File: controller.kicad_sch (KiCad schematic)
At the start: 17 parts, among them J701 Debug, SW701 RST, U701 STM32C031K6Tx

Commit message: Fix controller encoder bus names
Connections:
- net Encoder1.A renamed Encoder1.CLK
- net Encoder1.B renamed Encoder1.DAT
- net Encoder2.A renamed Encoder2.CLK
- net Encoder2.B renamed Encoder2.DAT
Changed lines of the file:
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@@
 		)
 	)
-	(label "Encoder1.B"
+	(label "Encoder1.DAT"
 		(at 161.29 81.28 0)
 		(effects
@@
 		)
 	)
-	(label "Encoder2.A"
+	(label "Encoder2.CLK"
 		(at 138.43 93.98 180)
 		(effects
@@
 		)
 	)
-	(label "Encoder2.B"
+	(label "Encoder2.DAT"
 		(at 138.43 96.52 180)
 		(effects
@@
 		)
 	)
-	(label "Encoder1.A"
+	(label "Encoder1.CLK"
 		(at 161.29 78.74 0)
 		(effects

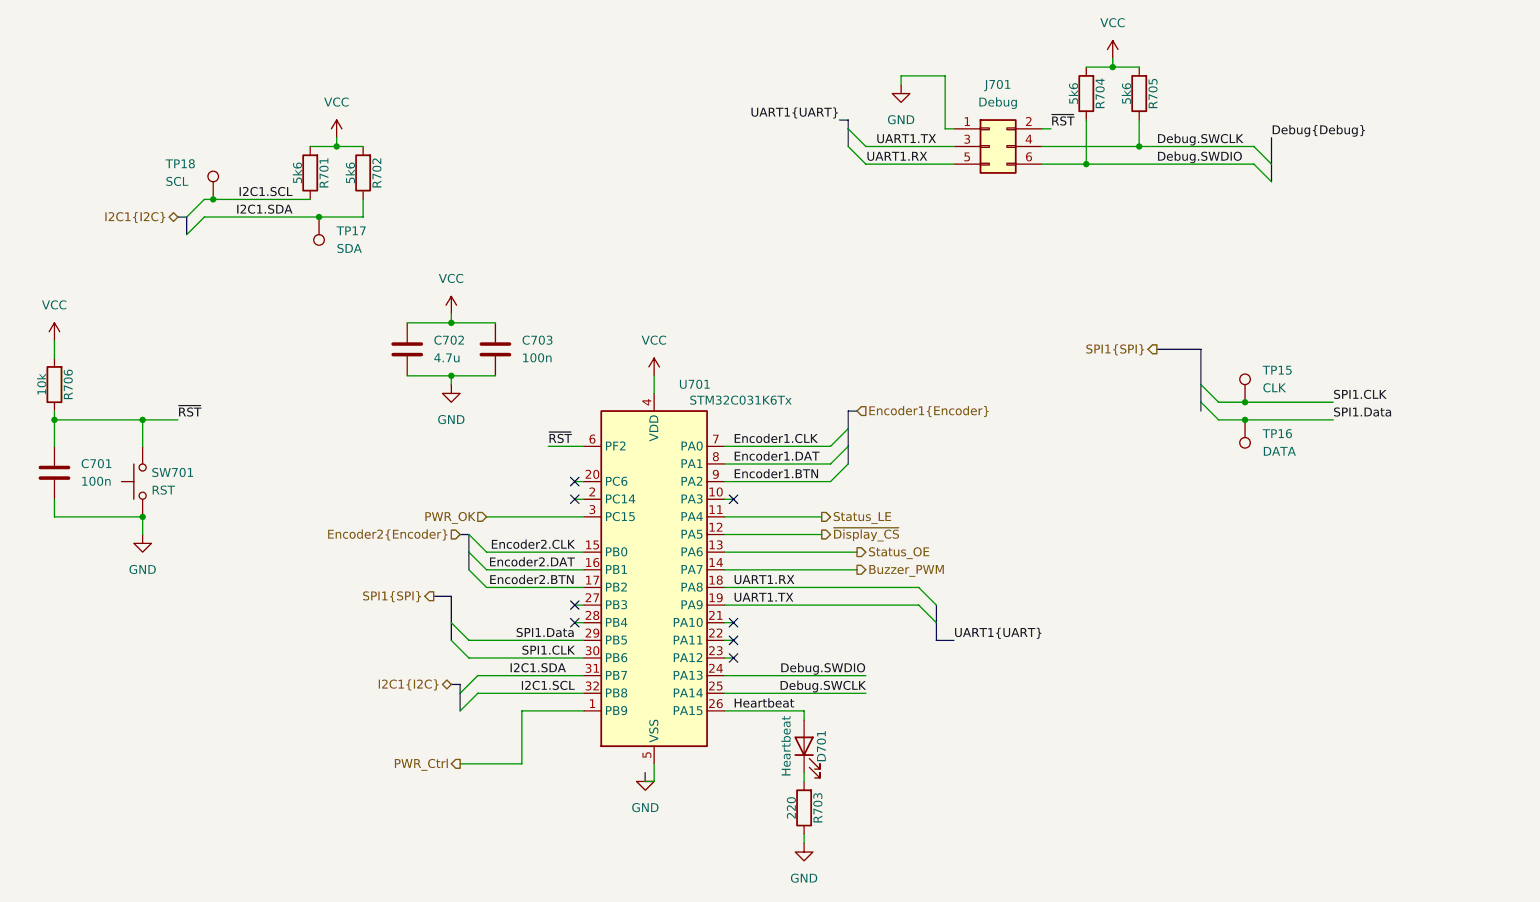
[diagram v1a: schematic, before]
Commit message: Reroute CPU for new display driving
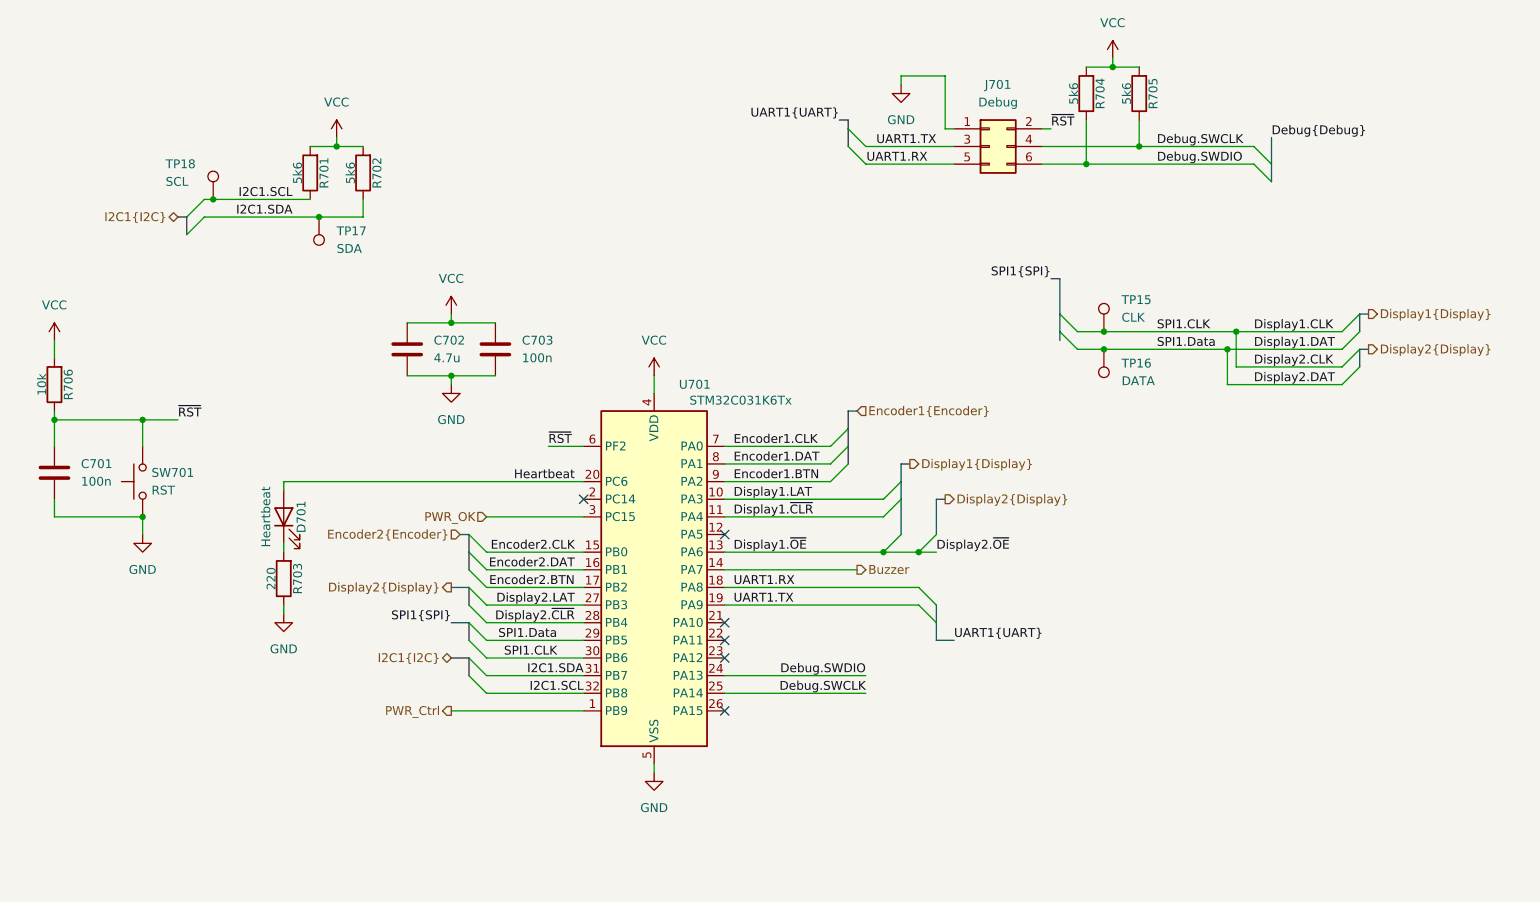
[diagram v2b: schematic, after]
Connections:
- net Heartbeat: now also U701.20 (PC6); no longer U701.26 (PA15)
- net Display1.LAT: now reaches U701.10 (PA3)
- net Display2.LAT: now reaches U701.27 (PB3)
- net Display2.~{CLR}: now reaches U701.28 (PB4)
- net Buzzer_PWM renamed Buzzer
- net SPI1.CLK renamed Display1.CLK
- net SPI1.Data renamed Display1.DAT
- net Status_LE renamed Display1.~{CLR}
- net Status_OE renamed Display1.~{OE}
- net ~{Display_CS}: no longer names the net of U701.12 (PA5)
- no-connect marks 8 -> 6
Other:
- moved on the sheet: D701, R703, TP15, TP16

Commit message: Assign component LCSC part numbers
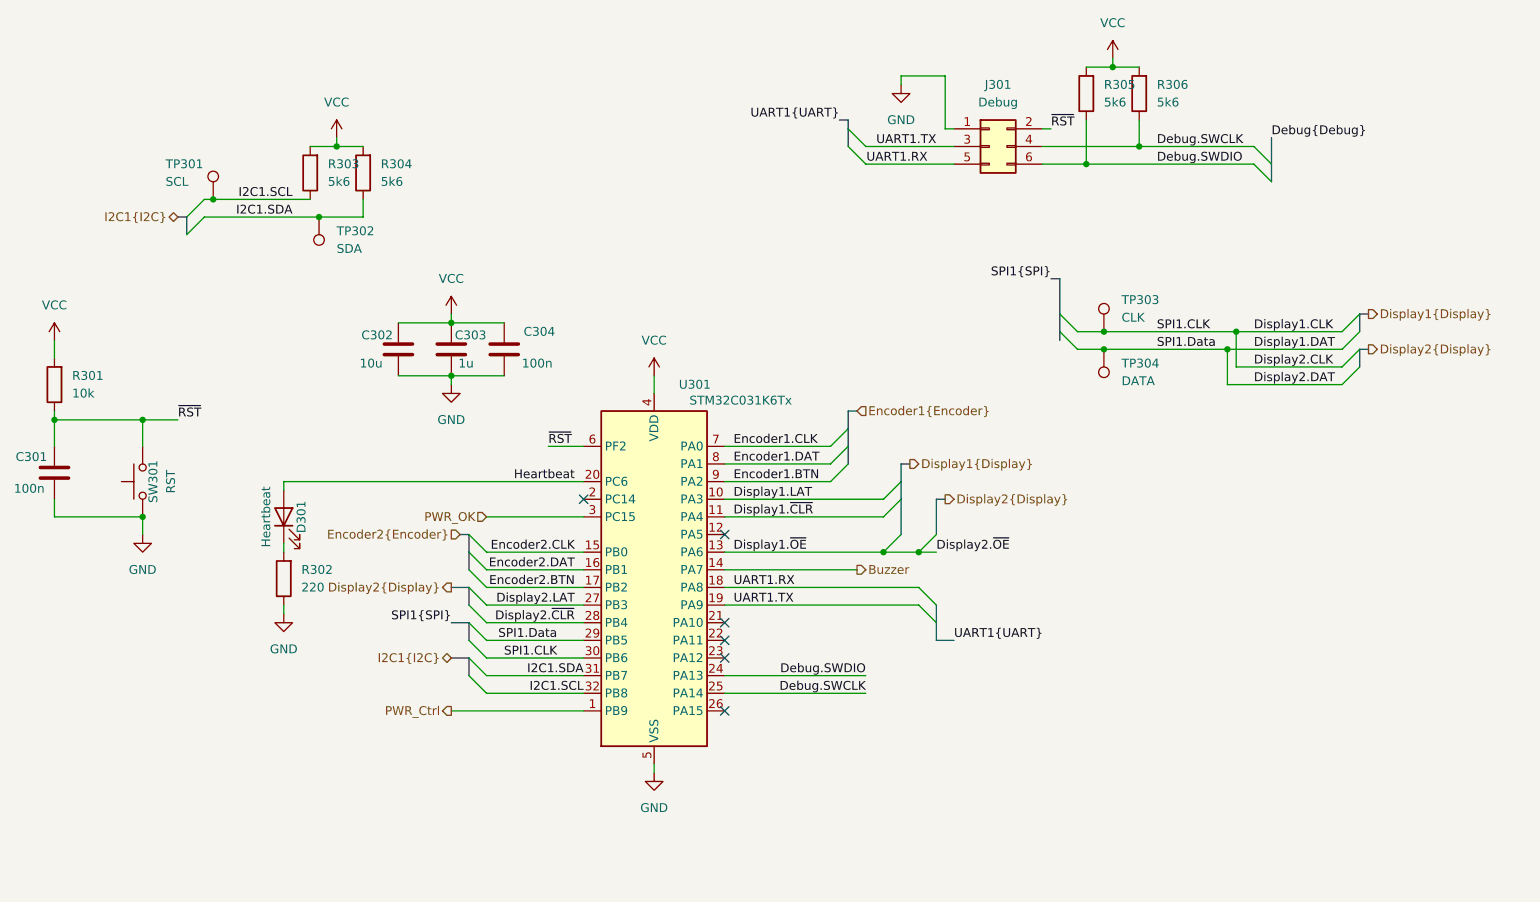
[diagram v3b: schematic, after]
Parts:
- removed C701, C703: 100n, Capacitor_SMD:C_1206_3216Metric_Pad1.33x1.80mm_HandSolder, symbol Device:C
- removed C702: 4.7u, Capacitor_SMD:C_1206_3216Metric_Pad1.33x1.80mm_HandSolder, symbol Device:C
- removed R701, R702, R704, R705: 5k6, Resistor_SMD:R_1206_3216Metric_Pad1.30x1.75mm_HandSolder, symbol Device:R
- removed R703: 220, Resistor_SMD:R_1206_3216Metric_Pad1.30x1.75mm_HandSolder, symbol Device:R
- removed R706: 10k, Resistor_SMD:R_1206_3216Metric_Pad1.30x1.75mm_HandSolder, symbol Device:R
- removed SW701: RST, Button_Switch_SMD:SW_SPST_PTS647_Sx38, symbol Switch:SW_Push
- added C301, C304: 100n, Capacitor_SMD:C_1206_3216Metric_Pad1.33x1.80mm_HandSolder, symbol Device:C
- added C302: 10u, Capacitor_SMD:C_1206_3216Metric_Pad1.33x1.80mm_HandSolder, symbol Device:C
- added C303: 1u, Capacitor_SMD:C_0805_2012Metric_Pad1.18x1.45mm_HandSolder, symbol Device:C
- added R301: 10k, Resistor_SMD:R_1206_3216Metric_Pad1.30x1.75mm_HandSolder, symbol Device:R
- added R302: 220, Resistor_SMD:R_1206_3216Metric_Pad1.30x1.75mm_HandSolder, symbol Device:R
- added R303, R304, R305, R306: 5k6, Resistor_SMD:R_1206_3216Metric_Pad1.30x1.75mm_HandSolder, symbol Device:R
- added SW301: RST, Button_Switch_THT:SW_PUSH_6mm, symbol Switch:SW_Push
- U301: renamed from U701; LCSC (none) -> C5456169
- renumbered D701 to D301, J701 to J301, TP18 to TP301, TP17 to TP302, TP15 to TP303, TP16 to TP304
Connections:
- net Debug.SWCLK: now also R306.1
- net Debug.SWDIO: now also R305.1
- net GND: now also C301.2, C302.2, C303.2, C304.2, R302.1, SW301.1
- net I2C1.SCL: now also R303.1
- net I2C1.SDA: now also R304.1
- net VCC: now also C302.1, C303.1, C304.1, R301.2, R303.2, R304.2, R305.2, R306.2
- net ~{RST}: now also C301.1, R301.1, SW301.2
- net at D301.1 (K): now also R302.2

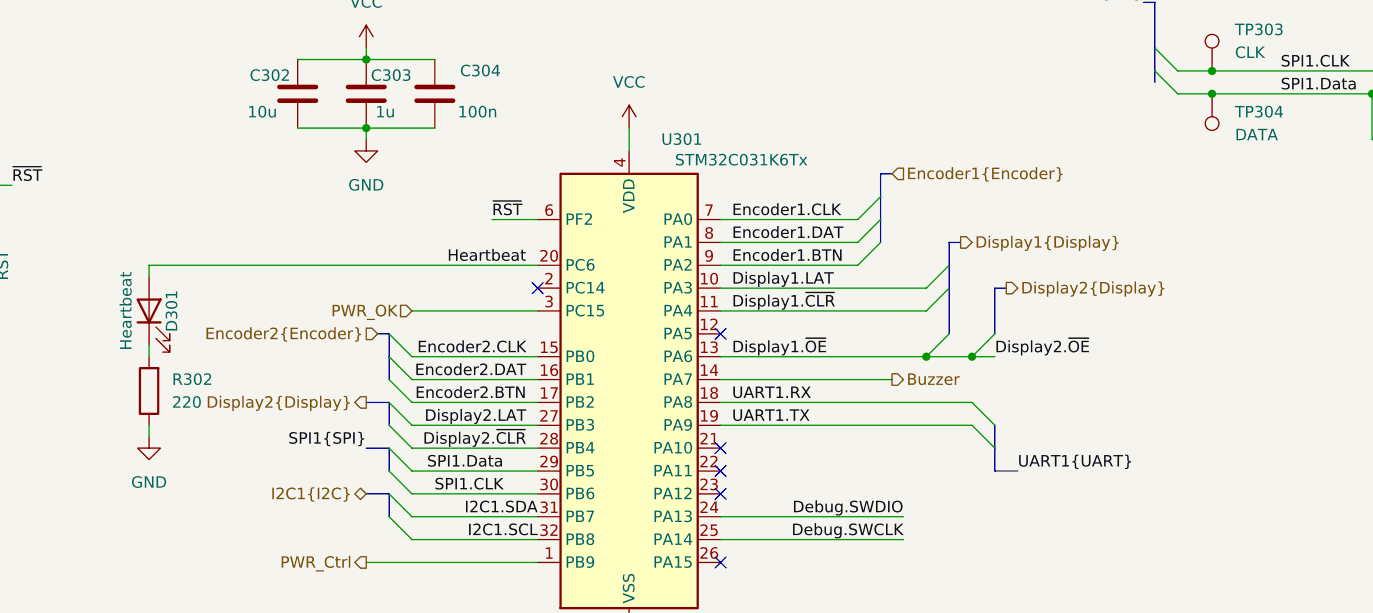
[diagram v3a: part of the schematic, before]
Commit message: Swapped pins for user elements to make routing easier
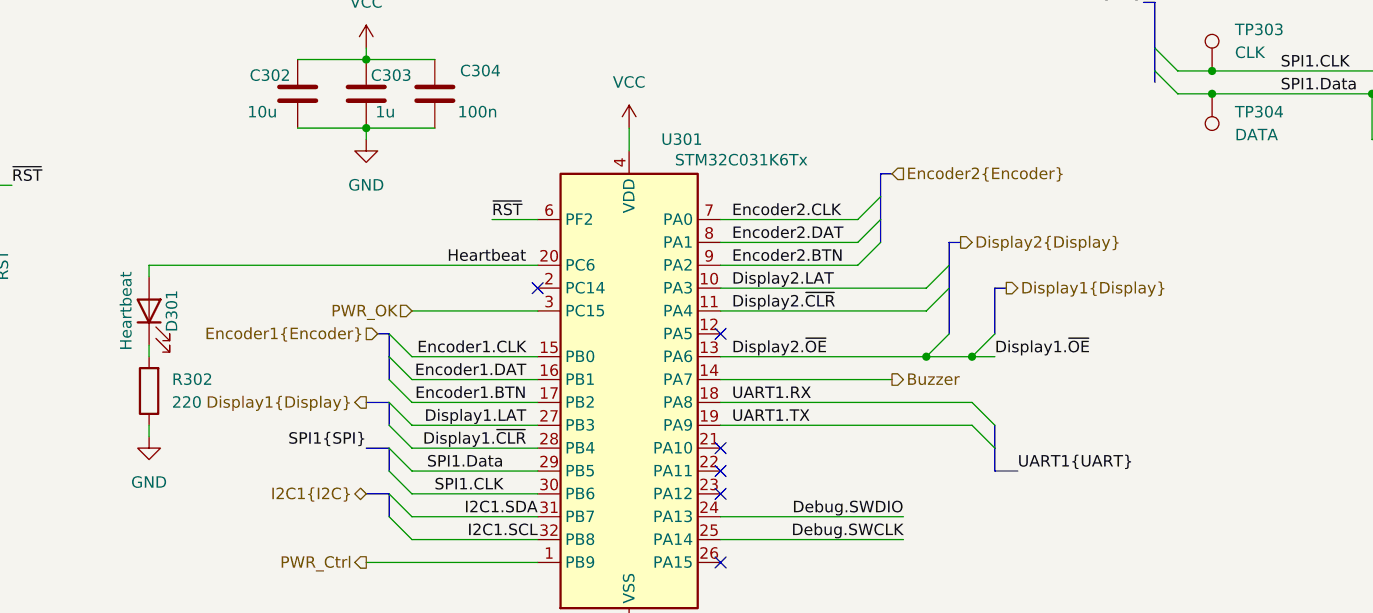
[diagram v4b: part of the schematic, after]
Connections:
- net Display1.LAT: now also U301.27 (PB3); no longer U301.10 (PA3)
- net Display1.~{CLR}: now also U301.28 (PB4); no longer U301.11 (PA4)
- net Display2.LAT: now also U301.10 (PA3); no longer U301.27 (PB3)
- net Display2.~{CLR}: now also U301.11 (PA4); no longer U301.28 (PB4)
- net Encoder1.BTN: now also U301.17 (PB2); no longer U301.9 (PA2)
- net Encoder1.CLK: now also U301.15 (PB0); no longer U301.7 (PA0)
- net Encoder1.DAT: now also U301.16 (PB1); no longer U301.8 (PA1)
- net Encoder2.BTN: now also U301.9 (PA2); no longer U301.17 (PB2)
- net Encoder2.CLK: now also U301.7 (PA0); no longer U301.15 (PB0)
- net Encoder2.DAT: now also U301.8 (PA1); no longer U301.16 (PB1)
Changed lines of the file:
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@@
 		)
 	)
-	(label "Display2.~{CLR}"
+	(label "Display1.~{CLR}"
 		(at 138.43 104.14 180)
 		(effects
@@
 		)
 	)
-	(label "Display2.LAT"
+	(label "Display1.LAT"
 		(at 138.43 101.6 180)
 		(effects
@@
 		)
 	)
-	(label "Encoder1.DAT"
+	(label "Encoder2.DAT"
 		(at 161.29 81.28 0)
 		(effects
@@
 		)
 	)
-	(label "Encoder2.CLK"
+	(label "Encoder1.CLK"
 		(at 138.43 93.98 180)
 		(effects
@@
 		)
 	)
-	(label "Encoder2.BTN"
+	(label "Encoder1.BTN"
 		(at 138.43 99.06 180)
 		(effects
@@
 		)
 	)
-	(label "Encoder2.DAT"
+	(label "Encoder1.DAT"
 		(at 138.43 96.52 180)
 		(effects
@@
 		)
 	)
-	(label "Display2.~{OE}"
+	(label "Display1.~{OE}"
 		(at 190.5 93.98 0)
 		(effects
@@
 		)
 	)
-	(label "Encoder1.BTN"
+	(label "Encoder2.BTN"
 		(at 161.29 83.82 0)
 		(effects
@@
 		)
 	)
-	(label "Display1.~{OE}"
+	(label "Display2.~{OE}"
 		(at 161.29 93.98 0)
 		(effects
@@
 		)
 	)
-	(label "Display1.LAT"
+	(label "Display2.LAT"
 		(at 161.29 86.36 0)
 		(effects
@@
 		)
 	)
-	(label "Display1.~{CLR}"
+	(label "Display2.~{CLR}"
 		(at 161.29 88.9 0)
 		(effects
@@
 		)
 	)
-	(label "Encoder1.CLK"
+	(label "Encoder2.CLK"
 		(at 161.29 78.74 0)
 		(effects
@@
 		)
 	)
+	(hierarchical_label "Display1{Display}"
+		(shape output)
+		(at 120.65 99.06 180)
+		(effects
+			(font
+				(size 1.27 1.27)
+			)
+			(justify right)
+		)
+	)
 	(hierarchical_label "Display2{Display}"
-		(shape output)
-		(at 120.65 99.06 180)
-		(effects
-			(font
-				(size 1.27 1.27)
-			)
-			(justify right)
-		)
-	)
-	(hierarchical_label "Display1{Display}"
 		(shape output)
 		(at 186.69 81.28 0)
@@
 		)
 	)
+	(hierarchical_label "Encoder2{Encoder}"
+		(shape input)
+		(at 179.07 73.66 0)
+		(effects
+			(font
+				(size 1.27 1.27)
+			)
+			(justify left)
+		)
+	)
 	(hierarchical_label "Encoder1{Encoder}"
 		(shape input)
-		(at 179.07 73.66 0)
+		(at 121.92 91.44 180)
+		(effects
+			(font
+				(size 1.27 1.27)
+			)
+			(justify right)
+		)
+	)
+	(hierarchical_label "Buzzer"
+		(shape output)
+		(at 179.07 96.52 0)
 		(effects
 			(font
@@
 		)
 	)
-	(hierarchical_label "Encoder2{Encoder}"
-		(shape input)
-		(at 121.92 91.44 180)
-		(effects
-			(font
-				(size 1.27 1.27)
-			)
-			(justify right)
-		)
-	)
-	(hierarchical_label "Buzzer"
-		(shape output)
-		(at 179.07 96.52 0)
-		(effects
-			(font
-				(size 1.27 1.27)
-			)
-			(justify left)
-		)
-	)
-	(hierarchical_label "Display2{Display}"
+	(hierarchical_label "Display1{Display}"
 		(shape output)
 		(at 191.77 86.36 0)

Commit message: Update BOM options for export
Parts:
- D301, J301, TP301, TP302, TP303, TP304: now left out of the parts list
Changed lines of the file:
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@@
 		(unit 1)
 		(exclude_from_sim no)
-		(in_bom yes)
+		(in_bom no)
 		(on_board yes)
 		(dnp no)
@@
 		(unit 1)
 		(exclude_from_sim no)
-		(in_bom yes)
+		(in_bom no)
 		(on_board yes)
 		(dnp no)
@@
 		(unit 1)
 		(exclude_from_sim no)
-		(in_bom yes)
+		(in_bom no)
 		(on_board yes)
 		(dnp no)
@@
 		(unit 1)
 		(exclude_from_sim no)
-		(in_bom yes)
+		(in_bom no)
 		(on_board yes)
 		(dnp no)
@@
 		(unit 1)
 		(exclude_from_sim no)
-		(in_bom yes)
+		(in_bom no)
 		(on_board yes)
 		(dnp no)
@@
 		(unit 1)
 		(exclude_from_sim no)
-		(in_bom yes)
-		(on_board yes)
-		(dnp no)
+		(in_bom no)
+		(on_board yes)
+		(dnp no)
